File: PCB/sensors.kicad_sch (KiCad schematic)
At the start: 7 parts, among them U2 SEN0395, U3 EKMC1603113, U4 TSL2591

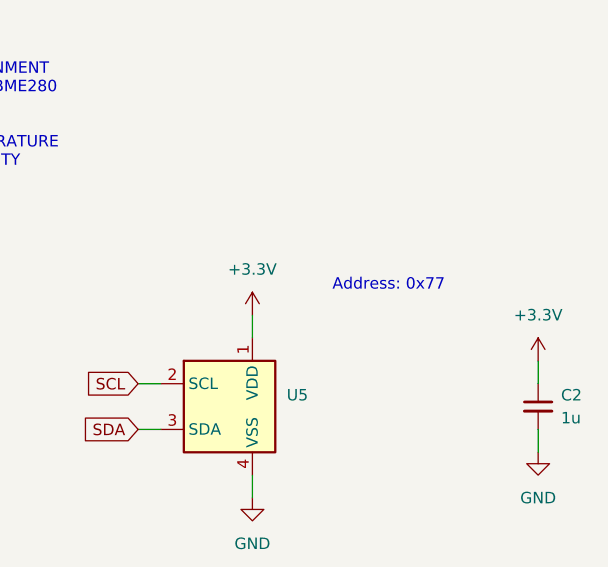
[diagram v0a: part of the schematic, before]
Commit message: Moved kicad files to the PCB folder
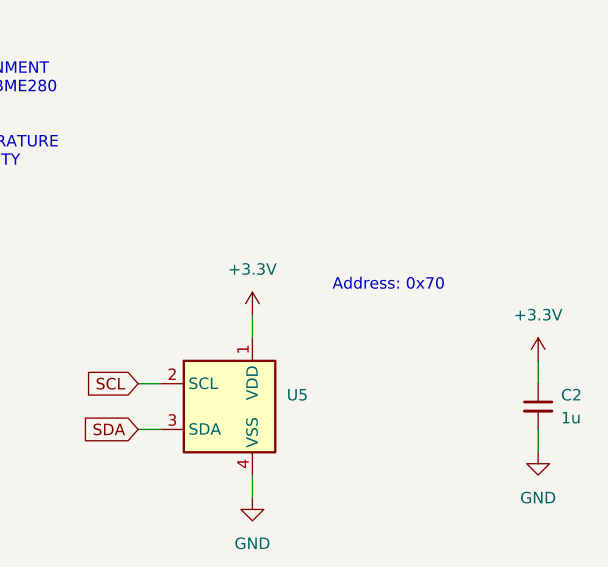
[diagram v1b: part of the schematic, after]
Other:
- note added: "Address: 0x70"
- note removed: "Address: 0x77"
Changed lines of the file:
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@@
     (effects (font (size 1.27 1.27)) (justify left bottom))
   )
-  (text "Address: 0x77" (at 224.79 48.26 0)
+  (text "Address: 0x70" (at 224.79 48.26 0)
     (effects (font (size 1.27 1.27)) (justify left bottom))
   )

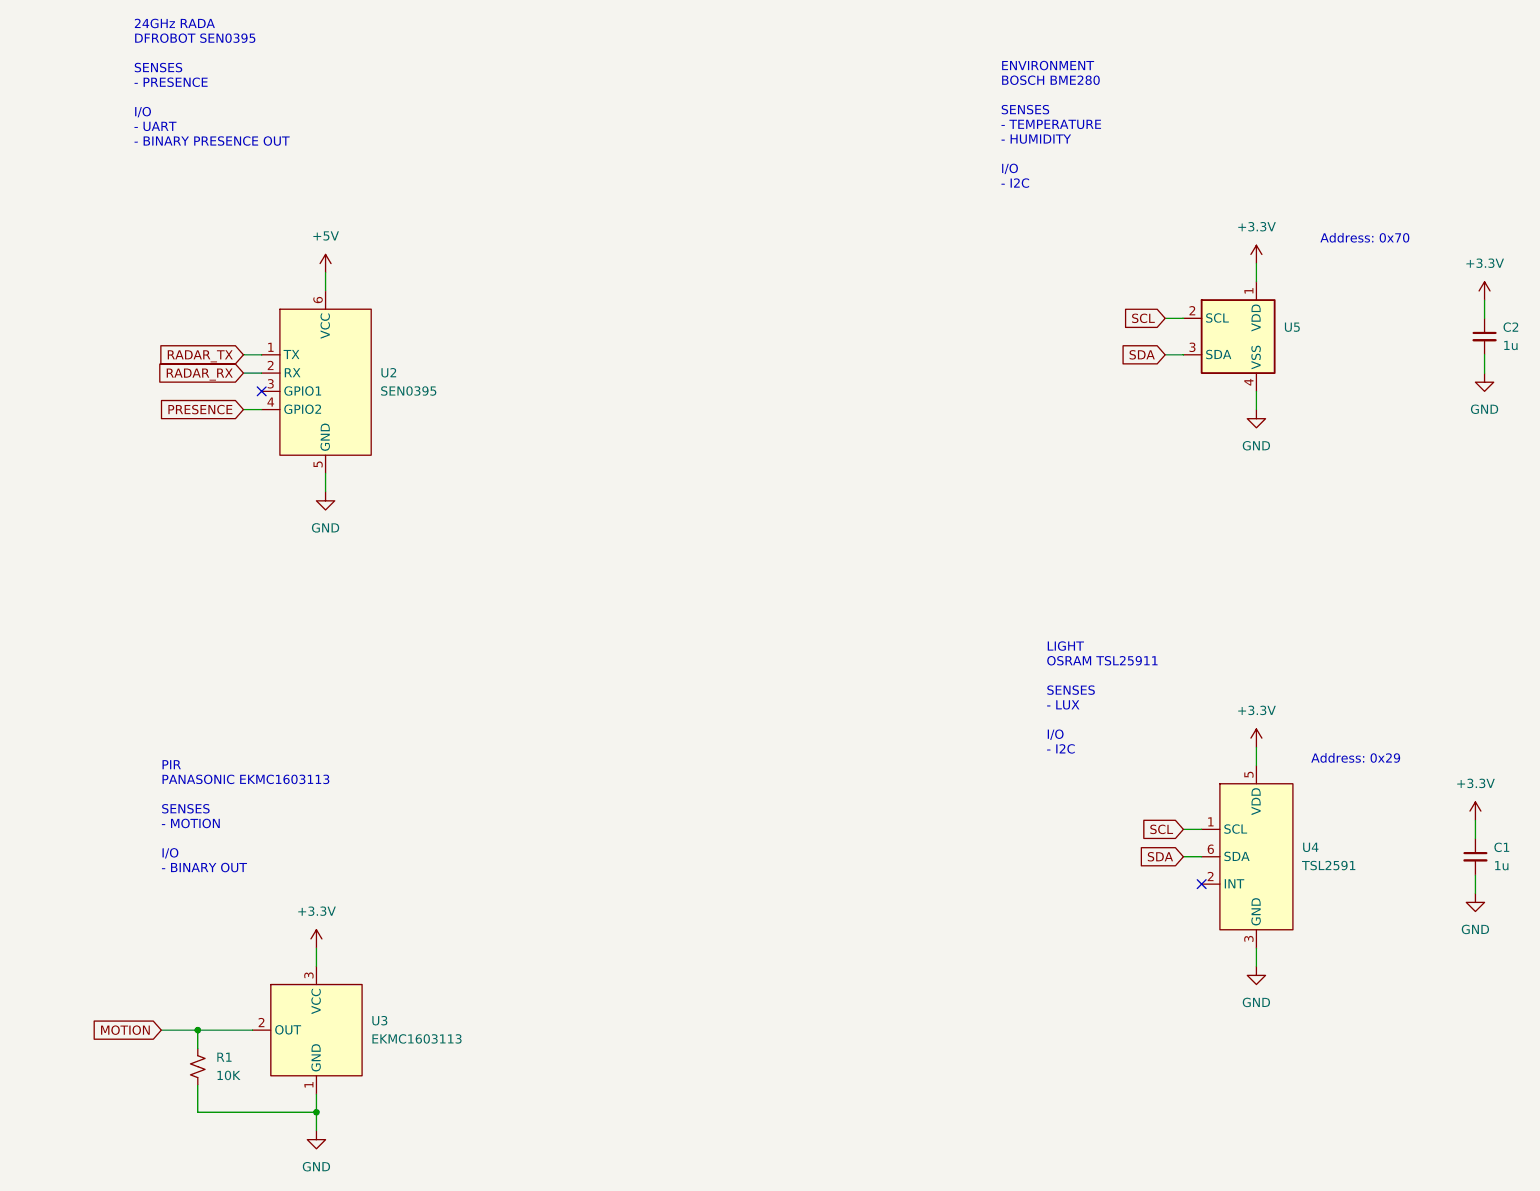
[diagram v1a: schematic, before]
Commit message: updated footprints and started board layout
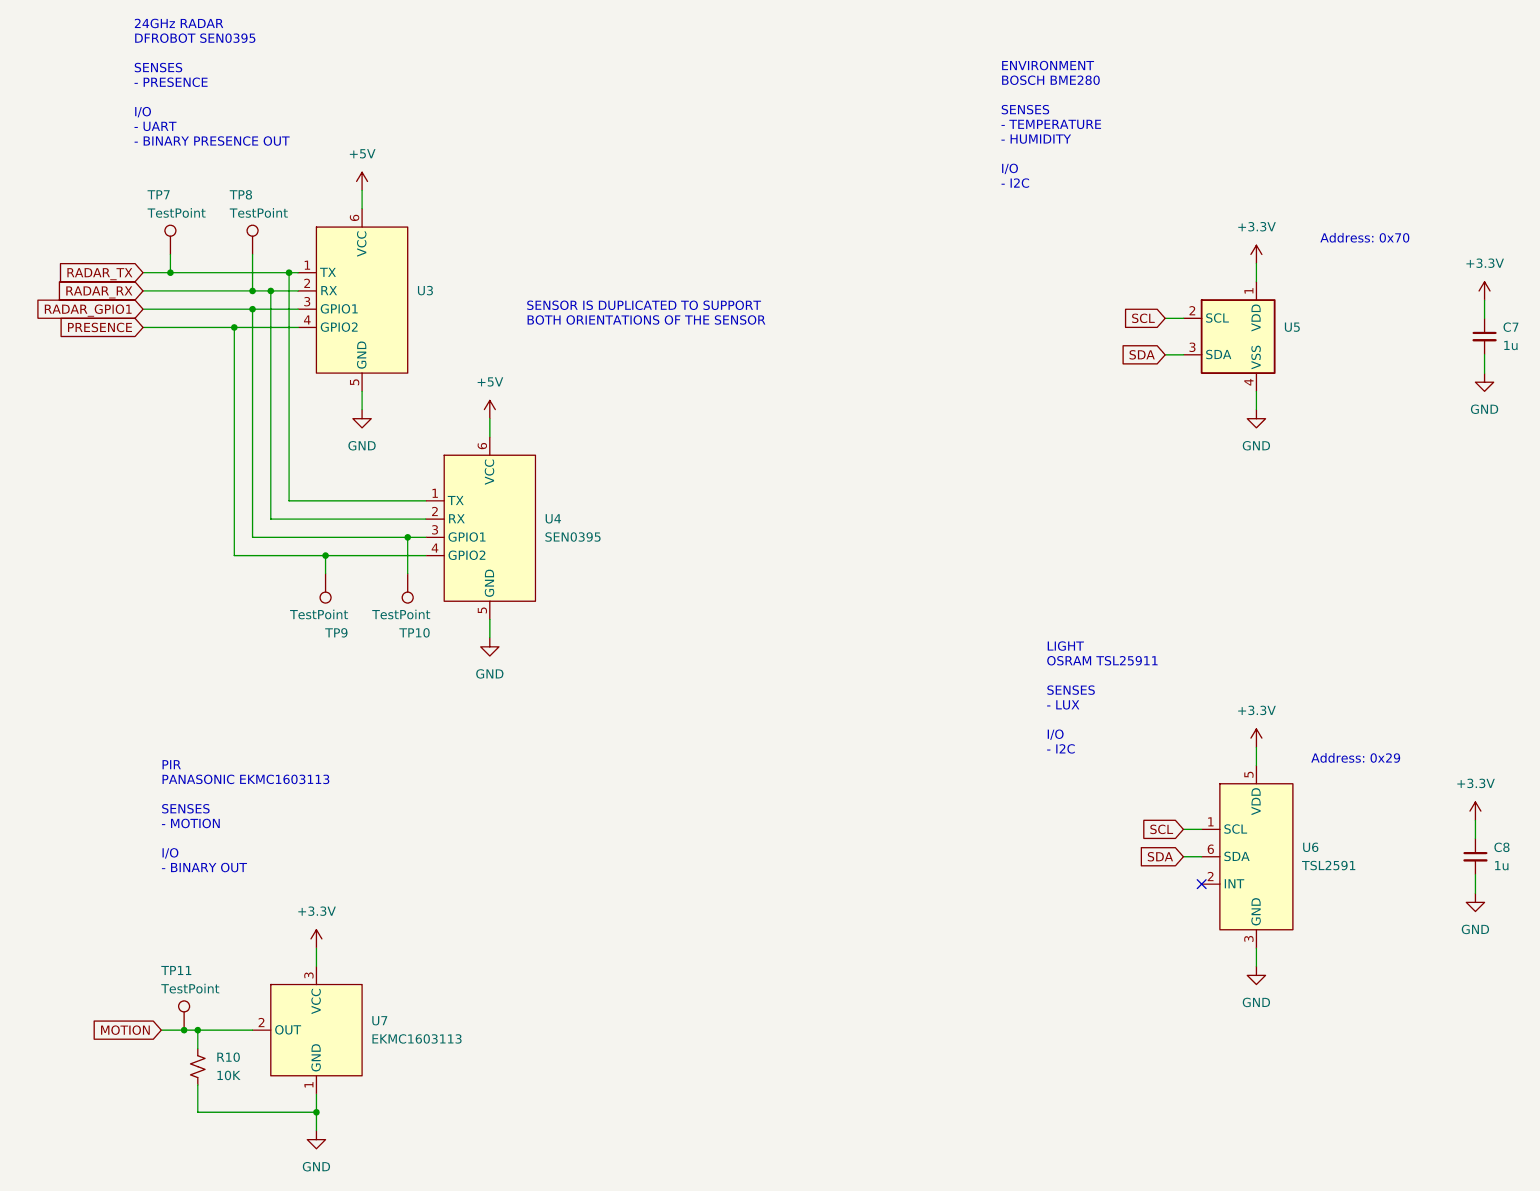
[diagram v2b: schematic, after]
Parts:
- added TP10, TP11, TP7, TP8, TP9: TestPoint, symbol Connector:TestPoint
- added U4: SEN0395, My Footprints:SEN0395, symbol My Symbols:SEN0395
- U3: renamed from U2; value SEN0395 -> (none); footprint My Footprints:SEN0395 -> (none)
- renumbered C2 to C7, C1 to C8, R1 to R10, U4 to U6, U3 to U7
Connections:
- net +5V: now also U4.6 (VCC)
- net GND: now also U5.5 (VSS), U4.5 (GND)
- net MOTION: now also TP11.1
- net PRESENCE: now also TP9.1, U4.4 (GPIO2)
- net RADAR_RX: now also TP8.1, U4.2 (RX)
- net RADAR_TX: now also TP7.1, U4.1 (TX)
- net RADAR_GPIO1: now reaches U3.3 (GPIO1)
- net RADAR_GPIO1: now also TP10.1, U4.3 (GPIO1)
- no-connect marks 2 -> 1
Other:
- note added: "24GHz RADAR DFROBOT SEN0395 SENSES - PRESENCE I/O - UART - BINARY PRESENCE OUT"
- note added: "SENSOR IS DUPLICATED TO SUPPORT BOTH ORIENTATIONS OF THE SENSOR"
- note removed: "24GHz RADA DFROBOT SEN0395 SENSES - PRESENCE I/O - UART - BINARY PRESENCE OUT"
- moved on the sheet: U3

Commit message: board layout work
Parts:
- TP5: renamed from TP7; footprint (none) -> TestPoint:TestPoint_THTPad_2.0x2.0mm_Drill1.0mm
- TP6: renamed from TP8; footprint (none) -> TestPoint:TestPoint_THTPad_2.0x2.0mm_Drill1.0mm
- TP7: renamed from TP9; footprint (none) -> TestPoint:TestPoint_THTPad_2.0x2.0mm_Drill1.0mm
- TP8: renamed from TP10; footprint (none) -> TestPoint:TestPoint_THTPad_2.0x2.0mm_Drill1.0mm
- TP9: renamed from TP11; footprint (none) -> TestPoint:TestPoint_THTPad_2.0x2.0mm_Drill1.0mm
- U3: value (none) -> SEN0395; footprint (none) -> My Footprints:SEN0395
- U4: renamed from U5; value (none) -> SHTC3; footprint (none) -> Sensor_Humidity:Sensirion_DFN-4-1EP_2x2mm_P1mm_EP0.7x1.6mm
- renumbered U4 to U5
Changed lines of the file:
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@@
   (symbol (lib_id "Connector:TestPoint") (at 97.79 93.98 180) (unit 1)
     (in_bom yes) (on_board yes)
-    (property "Reference" "TP10" (id 0) (at 100.965 102.235 0)
+    (property "Reference" "TP8" (id 0) (at 100.965 102.235 0)
       (effects (font (size 1.27 1.27)) (justify left))
     )
@@
       (effects (font (size 1.27 1.27)) (justify left))
     )
-    (property "Footprint" "" (id 2) (at 92.71 93.98 0)
+    (property "Footprint" "TestPoint:TestPoint_THTPad_2.0x2.0mm_Drill1.0mm" (id 2) (at 92.71 93.98 0)
       (effects (font (size 1.27 1.27)) hide)
     )
@@
   (symbol (lib_id "Connector:TestPoint") (at 76.2 49.53 0) (unit 1)
     (in_bom yes) (on_board yes)
-    (property "Reference" "TP8" (id 0) (at 73.025 41.275 0)
+    (property "Reference" "TP6" (id 0) (at 73.025 41.275 0)
       (effects (font (size 1.27 1.27)) (justify left))
     )
@@
       (effects (font (size 1.27 1.27)) (justify left))
     )
-    (property "Footprint" "" (id 2) (at 81.28 49.53 0)
+    (property "Footprint" "TestPoint:TestPoint_THTPad_2.0x2.0mm_Drill1.0mm" (id 2) (at 81.28 49.53 0)
       (effects (font (size 1.27 1.27)) hide)
     )
@@
   (symbol (lib_id "Connector:TestPoint") (at 86.36 93.98 180) (unit 1)
     (in_bom yes) (on_board yes)
-    (property "Reference" "TP9" (id 0) (at 89.535 102.235 0)
+    (property "Reference" "TP7" (id 0) (at 89.535 102.235 0)
       (effects (font (size 1.27 1.27)) (justify left))
     )
@@
       (effects (font (size 1.27 1.27)) (justify left))
     )
-    (property "Footprint" "" (id 2) (at 81.28 93.98 0)
+    (property "Footprint" "TestPoint:TestPoint_THTPad_2.0x2.0mm_Drill1.0mm" (id 2) (at 81.28 93.98 0)
       (effects (font (size 1.27 1.27)) hide)
     )
@@
   (symbol (lib_id "Connector:TestPoint") (at 66.675 157.48 0) (unit 1)
     (in_bom yes) (on_board yes)
-    (property "Reference" "TP11" (id 0) (at 63.5 149.225 0)
+    (property "Reference" "TP9" (id 0) (at 63.5 149.225 0)
       (effects (font (size 1.27 1.27)) (justify left))
     )
@@
       (effects (font (size 1.27 1.27)) (justify left))
     )
-    (property "Footprint" "" (id 2) (at 71.755 157.48 0)
+    (property "Footprint" "TestPoint:TestPoint_THTPad_2.0x2.0mm_Drill1.0mm" (id 2) (at 71.755 157.48 0)
       (effects (font (size 1.27 1.27)) hide)
     )
@@
       (effects (font (size 1.27 1.27)) (justify left))
     )
-    (property "Value" "" (id 1) (at 99.06 57.1499 0)
-      (effects (font (size 1.27 1.27)) (justify left))
-    )
-    (property "Footprint" "" (id 2) (at 91.44 39.37 0)
+    (property "Value" "SEN0395" (id 1) (at 99.06 57.1499 0)
+      (effects (font (size 1.27 1.27)) (justify left))
+    )
+    (property "Footprint" "My Footprints:SEN0395" (id 2) (at 91.44 39.37 0)
       (effects (font (size 1.27 1.27)) hide)
     )
@@
   (symbol (lib_id "Connector:TestPoint") (at 64.77 49.53 0) (unit 1)
     (in_bom yes) (on_board yes)
-    (property "Reference" "TP7" (id 0) (at 61.595 41.275 0)
+    (property "Reference" "TP5" (id 0) (at 61.595 41.275 0)
       (effects (font (size 1.27 1.27)) (justify left))
     )
@@
       (effects (font (size 1.27 1.27)) (justify left))
     )
-    (property "Footprint" "" (id 2) (at 69.85 49.53 0)
+    (property "Footprint" "TestPoint:TestPoint_THTPad_2.0x2.0mm_Drill1.0mm" (id 2) (at 69.85 49.53 0)
       (effects (font (size 1.27 1.27)) hide)
     )
@@
   (symbol (lib_id "My Symbols:SEN0395") (at 109.22 71.12 0) (unit 1)
     (in_bom yes) (on_board yes) (fields_autoplaced)
-    (property "Reference" "U4" (id 0) (at 116.84 86.3599 0)
+    (property "Reference" "U5" (id 0) (at 116.84 86.3599 0)
       (effects (font (size 1.27 1.27)) (justify left))
     )
@@
   (symbol (lib_id "Sensor_Humidity:SHTC3") (at 213.36 60.96 0) (unit 1)
     (in_bom yes) (on_board yes) (fields_autoplaced)
-    (property "Reference" "U5" (id 0) (at 219.71 59.6899 0)
-      (effects (font (size 1.27 1.27)) (justify left))
-    )
-    (property "Value" "" (id 1) (at 219.71 62.2299 0)
-      (effects (font (size 1.27 1.27)) (justify left))
-    )
-    (property "Footprint" "" (id 2) (at 218.44 69.85 0)
-      (effects (font (size 1.27 1.27)) hide)
-    )
+    (property "Reference" "U4" (id 0) (at 219.71 59.6899 0)
+      (effects (font (size 1.27 1.27)) (justify left))
+    )
+    (property "Value" "SHTC3" (id 1) (at 219.71 62.2299 0)
+      (effects (font (size 1.27 1.27)) (justify left))
+    )
+    (property "Footprint" "Sensor_Humidity:Sensirion_DFN-4-1EP_2x2mm_P1mm_EP0.7x1.6mm" (id 2) (at 218.44 69.85 0)
+      (effects (font (size 1.27 1.27)) hide)
+    )
